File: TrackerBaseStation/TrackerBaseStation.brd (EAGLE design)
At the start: 14 x 38.1 mm, 24 parts, among them J1 DF12A3.0-14DS, Q1 16MHz, U1 ATMEGA8U2MU, U2 RCLAMP0502A, U3 NRF24L01NOPAD, U4 BD2425NNRF0404, X1 USB-LEG

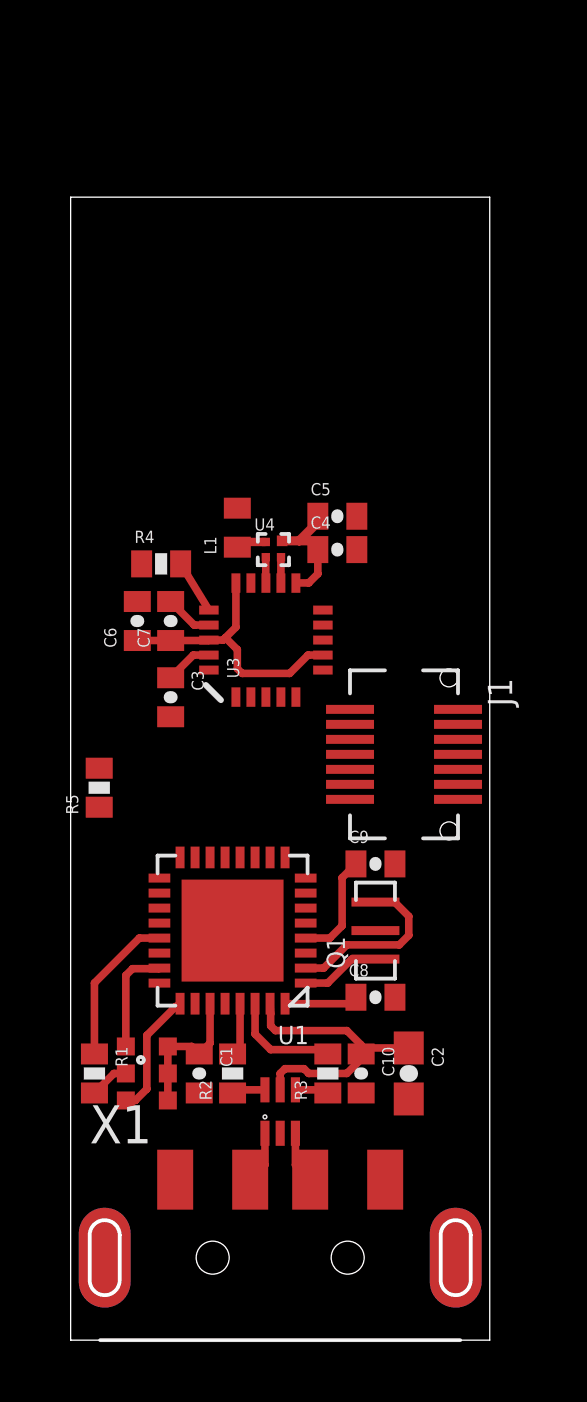
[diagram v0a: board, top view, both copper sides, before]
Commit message: with antenna
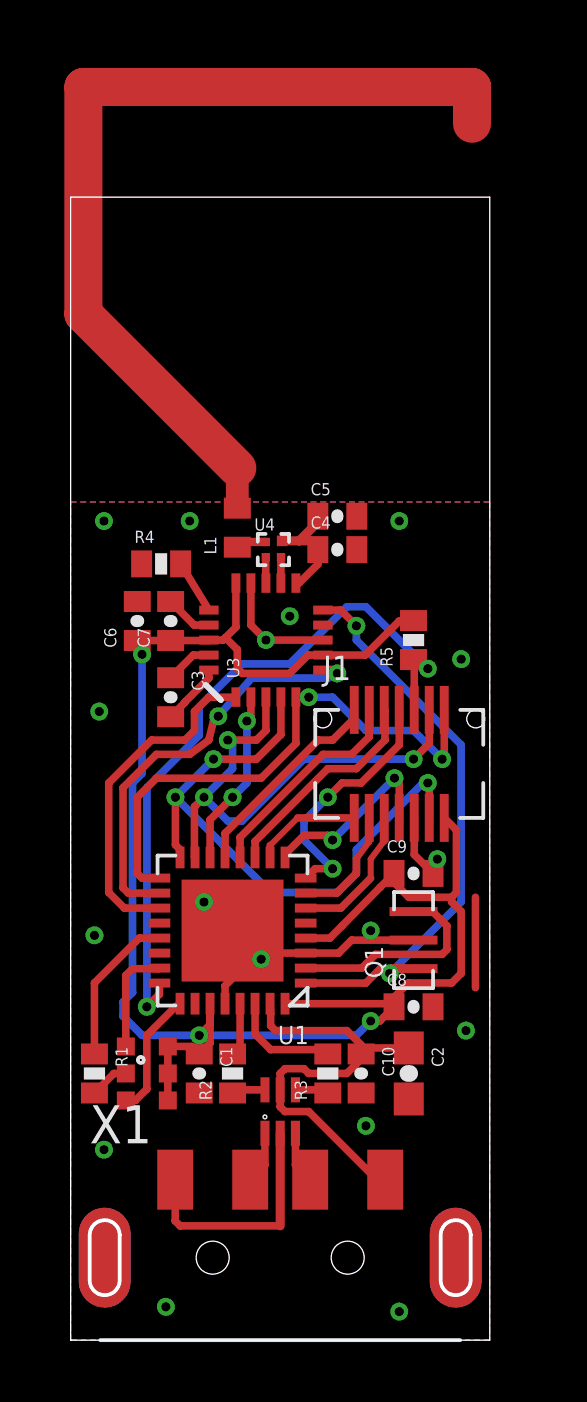
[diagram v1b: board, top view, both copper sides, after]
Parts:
- moved R5 11.6 mm to (11.4, 23.3)
- moved C9 1.31 mm to (11.4, 15.6)
- moved C8 1.31 mm to (11.4, 11.1)
- moved Q1 1.31 mm to (11.4, 13.3)
- moved J1 0.35 mm to (11.0, 19.2), turned to 0 degrees
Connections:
- net PD0: now also J1.10; no longer J1.9
- net PD1: now also J1.12; no longer J1.10
- net PD4: now also J1.14; no longer J1.11
- net PD5: now also J1.9; no longer J1.12
- net PD6: now also J1.11; no longer J1.13
- net PD7: now also J1.13; no longer J1.14
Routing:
- net +3V3: track 20.2 -> 59.7 mm, vias 0 -> 3
- net GND: track 1.60 -> 28.9 mm, vias 0 -> 15
- net RESET: track 0.00 -> 23.8 mm, vias 0 -> 2
- net MOSI: track 0.00 -> 20.8 mm, vias 0 -> 3
- net MISO: track 0.00 -> 18.4 mm, vias 0 -> 2
- net SCK: track 0.00 -> 17.1 mm, vias 0 -> 3
- net XTAL1: track 2.66 -> 19.4 mm, vias 0 -> 2
- net N$17: track 0.00 -> 14.1 mm, vias 0 -> 2
- net N$26: track 0.00 -> 13.0 mm
- net CE: track 0.00 -> 11.4 mm
- net RX: track 0.00 -> 8.40 mm, vias 0 -> 2
- net N$25: track 0.00 -> 7.57 mm
- net PD5: track 0.00 -> 7.28 mm
- net PD6: track 0.00 -> 7.26 mm
- net N$18: track 0.00 -> 7.26 mm
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- added copper zone on layer 1, net GND
- added copper zone on layer 16, net GND

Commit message: silkscreen
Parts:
- added U$1: (no value), adjacent-reality:ADJACENTREALITY-LOGO-0.35
- added U$2: (no value), SparkFun-Aesthetics:OSHW-LOGO-M
- moved C1 0.48 mm to (4.76, 8.89)
- moved C10 0.48 mm to (10.2, 8.89)
- moved C2 0.48 mm to (11.7, 8.89)
- moved C4 0.48 mm to (9.37, 26.4)
- moved C5 0.48 mm to (9.37, 27.5)
- moved C8 0.48 mm to (11.9, 11.1)
- moved C9 0.48 mm to (11.9, 15.6)
- moved J1 0.48 mm to (11.4, 19.2)
- moved Q1 0.48 mm to (11.9, 13.3)
- moved R2 0.48 mm to (5.87, 8.89)
- moved R3 0.48 mm to (9.05, 8.89)
- moved R4 0.48 mm to (3.49, 25.9)
- moved R5 0.48 mm to (11.9, 23.3)
- moved U1 0.48 mm to (5.87, 13.7)
- moved U3 0.48 mm to (6.99, 23.3)
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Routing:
- net ANT: track 0.00 -> 30.3 mm
- net N$26: track 13.0 -> 0.00 mm
- net N$25: track 7.57 -> 0.00 mm
- net N$18: track 7.26 -> 0.00 mm
- net N$27: track 1.23 -> 0.00 mm
- net N$14: track 1.13 -> 0.00 mm
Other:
- board size 14 x 38.1 mm -> 14.9 x 42.7 mm
- board text added: "Adjacent Reality"
- board text added: "Base Station 0.1"
- board text added: "Creative Commons By"
- board text added: "Nirav Patel <nrp@eclecti.cc>"
- board text added: "http://adjacentreality.org"
